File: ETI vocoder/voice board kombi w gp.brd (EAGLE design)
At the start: 160 x 60.3 mm, 174 parts, among them IC1 TL072P, IC1. TL072P, IC2 TL072P, IC2. TL072P, IC3 TL081P, IC3. TL081P, IC4 TL081P, IC4. TL081P, IC5 TL072P, IC6 LM13600AN, IC7 TL072P, IC7. TL072P, P1 C-OR-R050_075-025X100, P1. C-OR-R050_075-025X100, P10 C-OR-R050_075-025X100, P10. C-OR-R050_075-025X100, P11 C-OR-R050_075-025X100, P11. C-OR-R050_075-025X100, P12 C-OR-R050_075-025X100, P12. C-OR-R050_075-025X100, P13 C-OR-R050_075-025X100, P13. C-OR-R050_075-025X100, P14 C-OR-R050_075-025X100, P14. C-OR-R050_075-025X100, P15 C-OR-R050_075-025X100, P15. C-OR-R050_075-025X100, P16 C-OR-R050_075-025X100, P16. C-OR-R050_075-025X100, P2 C-OR-R050_075-025X100, P2. C-OR-R050_075-025X100, P3 C-OR-R050_075-025X100, P3. C-OR-R050_075-025X100, P4 C-OR-R050_075-025X100, P4. C-OR-R050_075-025X100, P5 C-OR-R050_075-025X100, P5. C-OR-R050_075-025X100, P6 C-OR-R050_075-025X100, P6. C-OR-R050_075-025X100, P7 C-OR-R050_075-025X100, P7. C-OR-R050_075-025X100, P8 C-OR-R050_075-025X100, P8. C-OR-R050_075-025X100, P9 C-OR-R050_075-025X100, P9. C-OR-R050_075-025X100, Q1 BF244C, Q1. BF244C, Q2 BC212L, Q2. BC212L

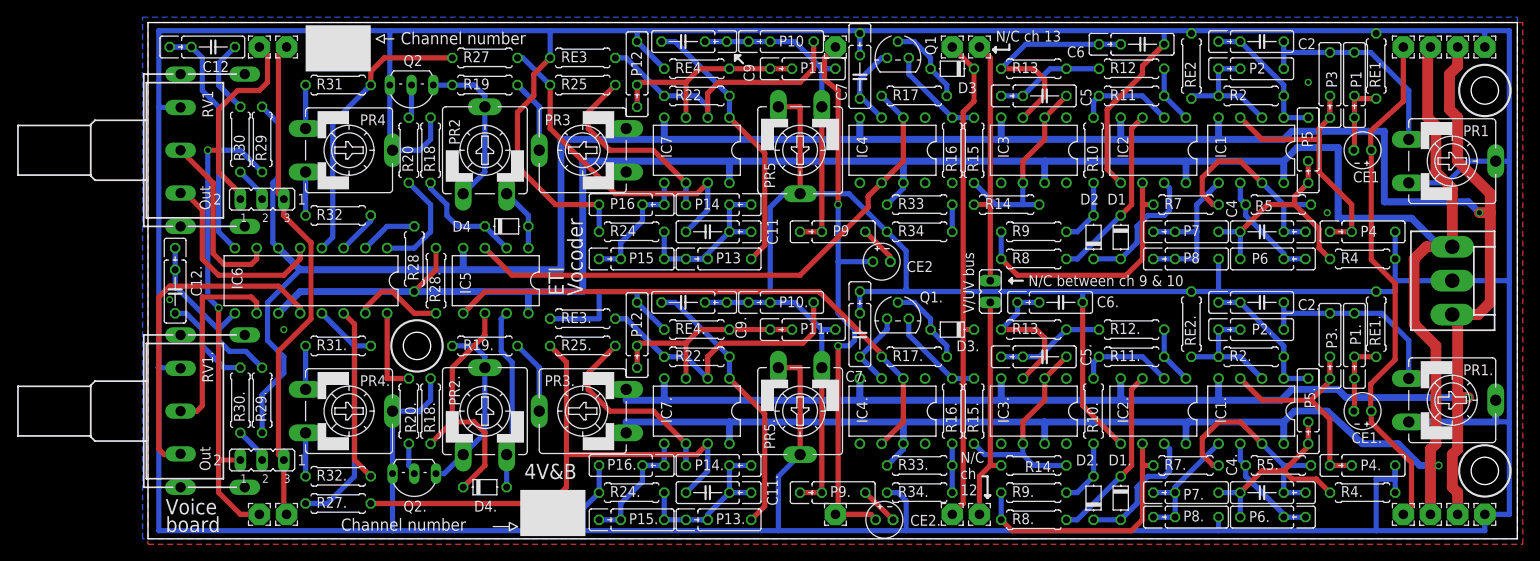
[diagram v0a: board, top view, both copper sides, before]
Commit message: Renamed components to better match parts list from the article. Any part that is not consistent across HP/LP/BP now has either CE, RE or P prefix
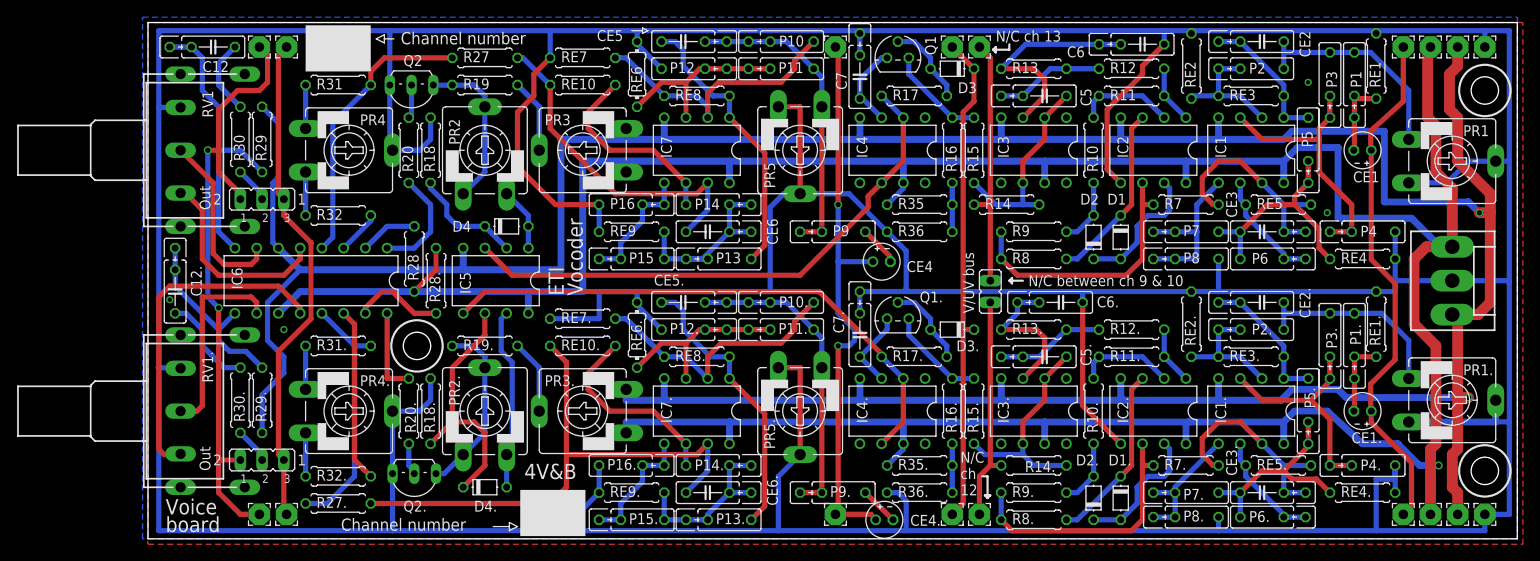
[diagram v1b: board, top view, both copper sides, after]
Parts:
- removed C2, C2.: (no value), joakim:C050_075-025X100J
- removed R2, R2., R4, R4.: (no value), resistor:0207/7
- added CE4, CE4.: (no value), resistor:E2-4
- added RE6, RE6.: (no value), resistor:0204/7
- added RE7, RE7.: (no value), resistor:0207/7
- CE2, CE2.: device resistor:E2-4 -> joakim:C050_075-025X100J
- moved RE4 80.9 mm to (141.9, 32.7), turned to 180 degrees
- moved RE4. 80.1 mm to (141.9, 5.40), turned to 180 degrees
- moved RE3 78.2 mm to (128.9, 51.8)
- moved RE3. 78.2 mm to (128.9, 21.3)
- moved CE2 51.4 mm to (130.2, 58.1), turned to 180 degrees
- moved CE2. 50.9 mm to (130.2, 27.6), turned to 180 degrees
- moved P12 6.70 mm to (63.8, 54.9), turned to 0 degrees
- moved P12. 6.70 mm to (63.8, 24.4), turned to 0 degrees
- moved P11 2.54 mm to (74.0, 54.9)
- moved P11. 2.54 mm to (74.0, 24.4)
- renumbered C11 to CE6, C11. to CE6., C4 to CE3, C4. to CE3., C9 to CE5, C9. to CE5., R22 to RE8, R22. to RE8., R24 to RE9, R24. to RE9., R25 to RE10, R25. to RE10., R33 to R35, R33. to R35., R34 to R36, R34. to R36., R5 to RE5, R5. to RE5.
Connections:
- net EXCITATION_IN: now also CE4.+, CE4..+; no longer CE2.+, CE2..+
- net GND: now also RE6..1, RE6.1, RE7..1, RE7.1; no longer R4..1, R4.1, RE3..1, RE3.1
- net N$1: now also RE3.1; no longer R2.1
- net N$2: now also CE2.1; no longer C2.1
- net N$29: now also RE7.2; no longer RE3.2
- net N$3: now also CE2.2, CE2.3, RE3.2; no longer C2.2, C2.3, R2.2
- net N$45: now also CE4.-; no longer CE2.-
- net N$46: now also RE6.2; no longer RE4.2
- net N$47: now also RE3..1; no longer R2..1
- net N$48: now also CE2..1; no longer C2..1
- net N$49: now also CE2..2, CE2..3, RE3..2; no longer C2..2, C2..3, R2..2
- net N$5: now also RE4.2; no longer R4.2
- net N$50: now also RE4..2; no longer R4..2
- net N$75: now also RE7..2; no longer RE3..2
- net N$90: now also CE4..-; no longer CE2..-
- net N$91: now also RE6..2; no longer RE4..2
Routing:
- net N$91: track 25.6 -> 21.5 mm
- net N$46: track 25.6 -> 21.5 mm
- net BIAS: track 3.18 -> 5.72 mm
- net N$27: track 38.1 -> 36.0 mm
- net N$73: track 38.1 -> 36.0 mm
- net N$75: track 33.3 -> 31.8 mm
- net N$76: track 32.0 -> 33.3 mm
- net N$29: track 34.0 -> 32.7 mm
- net N$30: track 32.0 -> 33.1 mm
- net EXCITATION_IN: track 67.6 -> 66.6 mm

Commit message: Separated LP/BP from BP/HP channels (left channel is never HP, right is never LP). Removed unused/shorted parts. Replaced all caps with wider ones w. 5mm pitch (may have to make them even wider). Replaced parts in left/right channel that had P footprints with R or C if they are now only one type combined with either N/C or short.
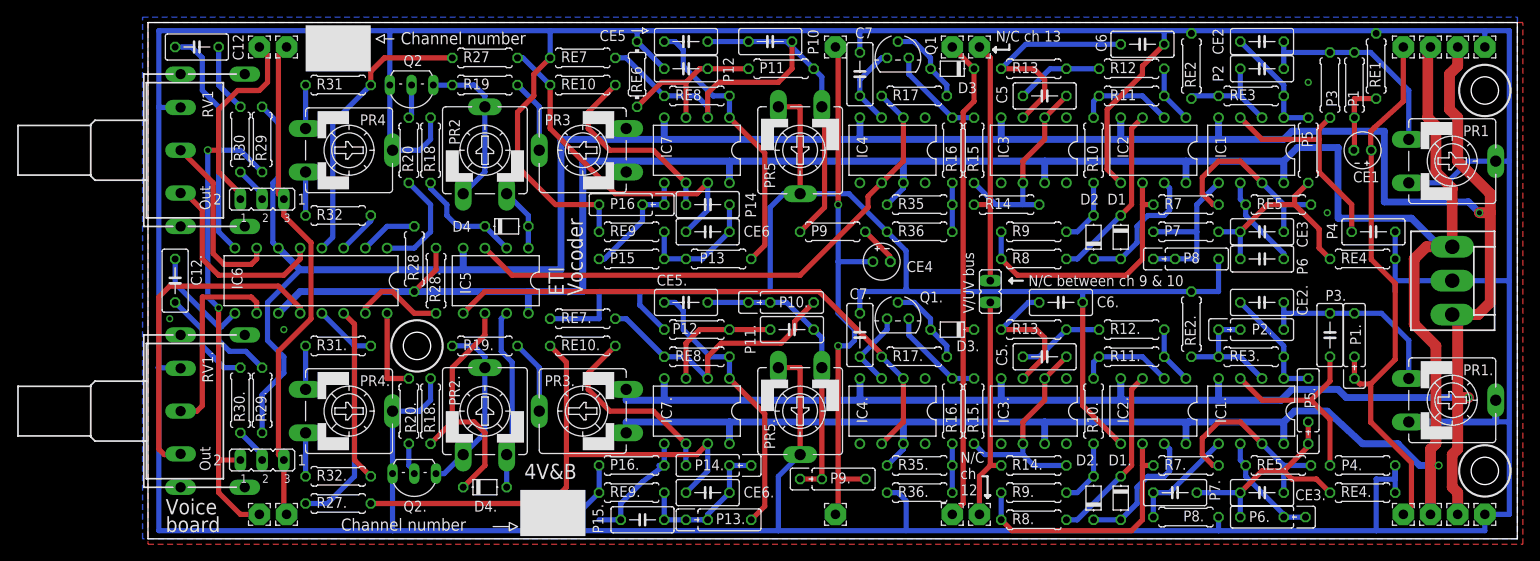
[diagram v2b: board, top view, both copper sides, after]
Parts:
- removed CE1., CE4.: (no value), resistor:E2-4
- removed RE1.: (no value), resistor:0207/7
- removed RE6.: (no value), resistor:0204/7
- C12, C12., C5, C5., C6, C6., C7, C7., CE2, CE2., CE3, CE3., CE5, CE5., CE6, CE6.: device joakim:C050_075-025X100J -> resistor:C050-030X075
- P1, P11, P12., P13, P15, P16., P3, P4., P5, P7, P8., P9: value C-OR-R050_075-025X100 -> (none); device joakim:P050_075-025X100J -> resistor:0207/7
- P10, P11., P12, P14, P15., P2, P3., P4, P6, P7.: value C-OR-R050_075-025X100 -> (none); device joakim:P050_075-025X100J -> resistor:C050-030X075
- moved C12 1.91 mm to (5.71, 57.5)
- moved P9. 1.59 mm to (80.0, 6.99)
- moved P10 1.27 mm to (72.7, 58.1)
- moved P2 1.27 mm to (130.2, 54.9)
- moved C12. 1.27 mm to (3.17, 30.2)
- moved P3. 1.27 mm to (138.1, 23.8)
- moved P11. 1.27 mm to (75.2, 24.4)
- moved P14 1.27 mm to (65.4, 39.1)
- moved P15. 1.27 mm to (57.8, 2.22)
- moved P7. 1.27 mm to (120.0, 5.40)
- moved P4 1.27 mm to (143.2, 35.9)
- moved P6 1.27 mm to (130.2, 32.7)
- moved P12 0.95 mm to (62.9, 54.9)
- moved CE5 0.32 mm to (62.9, 58.1)
- moved CE5. 0.32 mm to (62.9, 27.6)
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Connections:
- removed net N$88: CE1..-, P1..2, P1..3, RE1..2
- removed net N$90: CE4..-, P9..1
- net EXCITATION_IN: now also P9..1; no longer CE4..+
- net GND: no longer C7..3, C7.3, RE1..1, RE6..1
- net N$1: no longer P2.3
- net N$14: no longer C5.3
- net N$16: no longer C6.3
- net N$27: no longer CE5.3, P10.3, P9.3
- net N$28: no longer CE6.3, P13.3, P14.3
- net N$3: no longer CE2.3
- net N$32: no longer P15.3
- net N$33: no longer C12.3
- net N$43: no longer P1.3
- net N$44: no longer P3.3, P4.3
- net N$46: no longer P11.3, P12.3
- net N$49: no longer CE2..3
- net N$5: no longer P5.3
- net N$52: no longer P7..3, P8..3
- net N$53: no longer CE3..3
- net N$6: no longer P6.3
- net N$60: no longer C5..3
- net N$62: no longer C6..3
- net N$7: no longer P7.3
- net N$73: no longer CE5..3
- net N$74: no longer CE6..3
- net N$8: no longer CE3.3
- net N$84: no longer C12..3
- net N$87: no longer P15..3, P16..3
- net N$89: no longer P3..3, P4..3
- net N$91: no longer P11..3, P12..3, RE6..2
- net SPEECH_IN: now also P1..2, P1..3; no longer CE1..+
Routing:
- net GND: track 814.6 -> 793.8 mm
- net N$88: track 8.95 -> 0.00 mm
- net N$28: track 23.5 -> 15.3 mm
- net N$91: track 21.5 -> 14.6 mm
- net N$44: track 30.8 -> 25.7 mm
- net SPEECH_IN: track 61.3 -> 66.0 mm
- net N$90: track 4.54 -> 0.00 mm
- net N$52: track 15.8 -> 12.8 mm
- net N$74: track 21.4 -> 18.8 mm
- net N$60: track 12.7 -> 10.2 mm
- net N$49: track 16.4 -> 13.9 mm
- net N$3: track 16.4 -> 13.9 mm
- net N$14: track 12.7 -> 10.2 mm
- net N$1: track 15.3 -> 12.8 mm
- net N$5: track 27.2 -> 24.6 mm
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
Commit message: Changed all caps and C-or-Rs for 5mm pitch 3mm wide ones
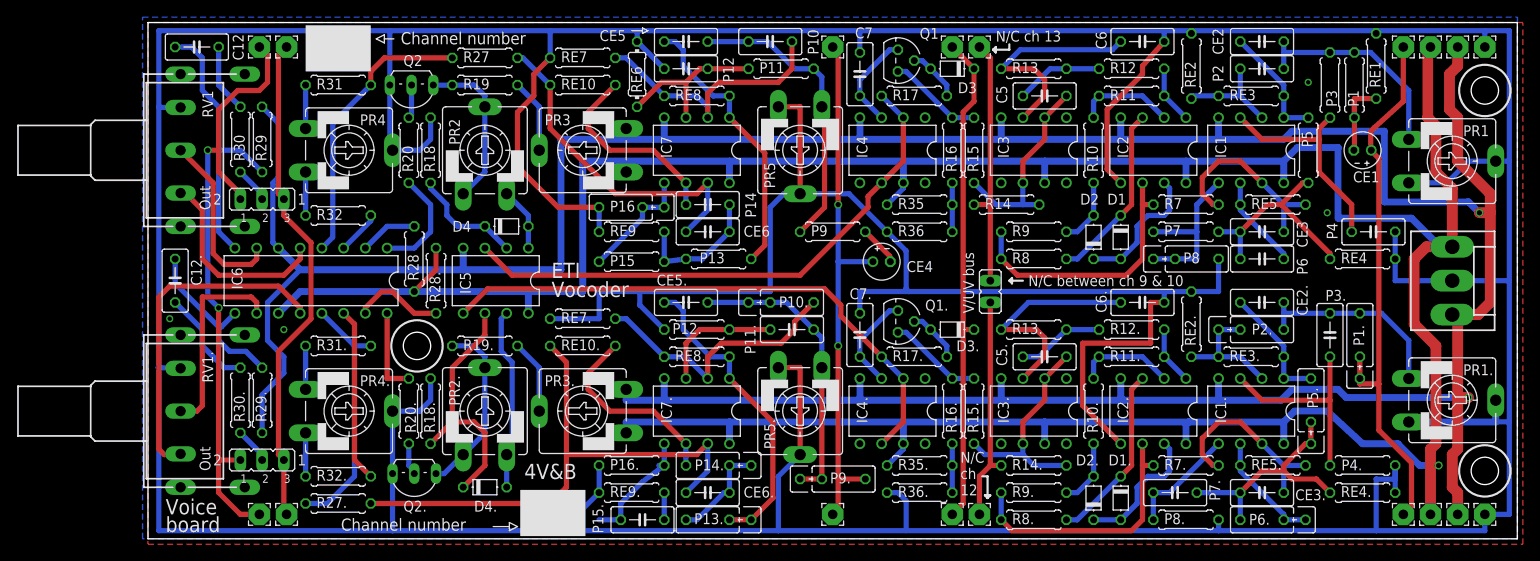
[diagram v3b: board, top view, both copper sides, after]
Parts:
- P1., P10., P13., P14., P16, P2., P5., P6., P8, P9.: value C-OR-R050_075-025X100 -> C-OR-R050_075-030X100; device joakim:P050_075-025X100J -> joakim:P050_075-030X100J
- moved C6. 9.52 mm to (116.2, 27.6)
- moved RE5 0.64 mm to (131.4, 39.1)
- moved RE5. 0.64 mm to (131.4, 8.57)
- moved P1. 0.63 mm to (141.6, 22.5)
- moved C6 0.32 mm to (116.2, 58.1)
- moved P15 0.32 mm to (56.5, 32.4)
- moved P16 0.32 mm to (56.5, 38.7)
- moved Q1. 0.32 mm to (87.6, 25.4), turned to 270 degrees
- moved P6. 0.32 mm to (131.4, 2.22)
- moved P8. 0.32 mm to (121.3, 2.22)
- moved P5. 0.32 mm to (135.9, 14.9)
- moved PAD3 0.32 mm to (80.0, 57.5)
- moved PAD4 0.32 mm to (80.0, 2.86)
- moved Q1 0.32 mm to (87.6, 55.9), turned to 270 degrees
- turned P13. to 0 degrees
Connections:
- new net N$88: P15..1, RE9..2
- net N$74: now also P13..1; no longer P13..2, P13..3, P15..1, RE9..2
- net N$76: now also P13..2, P13..3; no longer P13..1
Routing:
- net N$62: track 17.0 -> 26.6 mm
- net GND: track 793.8 -> 801.4 mm
- net N$74: track 18.8 -> 12.1 mm
- net N$65: track 9.83 -> 6.26 mm
- net N$19: track 9.83 -> 6.26 mm
- net N$76: track 33.0 -> 36.3 mm
- net N$88: track 0.00 -> 3.17 mm
- net N$64: track 9.35 -> 11.4 mm
- net SPEECH_IN: track 66.0 -> 64.3 mm
- net EXCITATION_IN: track 64.8 -> 63.1 mm
- net N$18: track 9.72 -> 11.4 mm
- net N$66: track 65.6 -> 66.4 mm
- net N$50: track 27.4 -> 28.2 mm
- net N$8: track 23.1 -> 22.5 mm
- net N$53: track 23.1 -> 22.5 mm
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
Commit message: Finished capacitor spacing tweaks, ic sockets should fit now
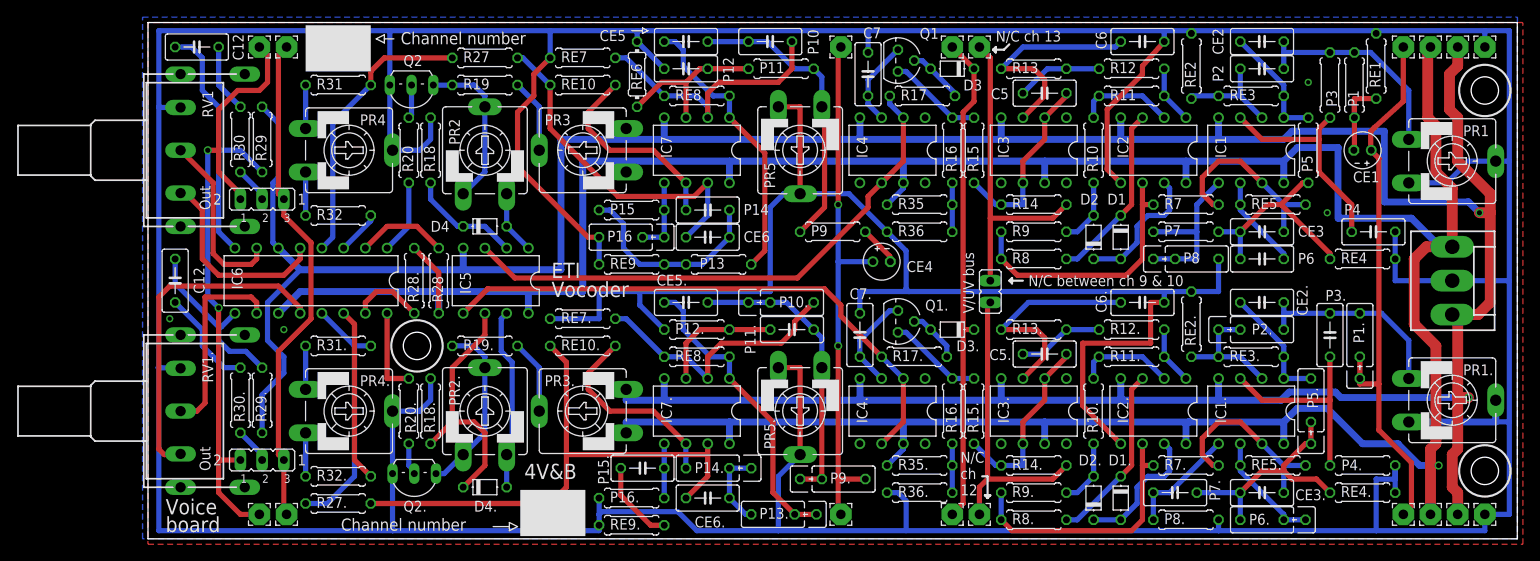
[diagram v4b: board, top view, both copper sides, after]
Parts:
- moved P13. 7.65 mm to (74.3, 2.86)
- moved P15. 6.03 mm to (57.8, 8.26), turned to 0 degrees
- moved P15 6.03 mm to (56.5, 38.4), turned to 0 degrees
- moved R28 3.82 mm to (34.0, 30.2)
- moved RE9. 3.81 mm to (56.5, 1.59)
- moved P16. 3.81 mm to (56.5, 4.76)
- moved RE9 3.81 mm to (56.5, 32.1)
- moved P16 3.49 mm to (56.5, 35.2)
- moved R14 3.17 mm to (103.5, 39.1), turned to 0 degrees
- moved R28. 2.54 mm to (31.1, 30.2)
- moved D4 2.54 mm to (39.4, 36.5)
- moved C7 0.95 mm to (84.1, 54.3)
- moved PAD3 0.95 mm to (81.0, 57.5)
- moved PAD4 0.95 mm to (81.0, 2.86)
- moved R17 0.95 mm to (90.5, 51.8)
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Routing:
- net VU_DETECTOR_2: track 26.6 -> 35.2 mm
- net N$28: track 15.6 -> 24.0 mm
- net N$87: track 14.4 -> 6.35 mm
- net VU_DETECTOR: track 29.7 -> 37.4 mm
- net N$88: track 3.17 -> 9.70 mm
- net +12V: track 368.9 -> 374.4 mm
- net N$32: track 13.9 -> 8.89 mm
- net N$40: track 12.6 -> 8.67 mm
- net N$38: track 6.77 -> 10.7 mm
- net N$61: track 25.4 -> 21.9 mm
- net N$74: track 12.1 -> 9.36 mm
- net N$80: track 10.7 -> 8.56 mm
- net N$15: track 23.5 -> 21.9 mm
- net N$18: track 11.4 -> 10.0 mm
- net GND: track 801.4 -> 800.4 mm
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
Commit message: Centered capacitors on resistors for a (hopefully) more tidy look
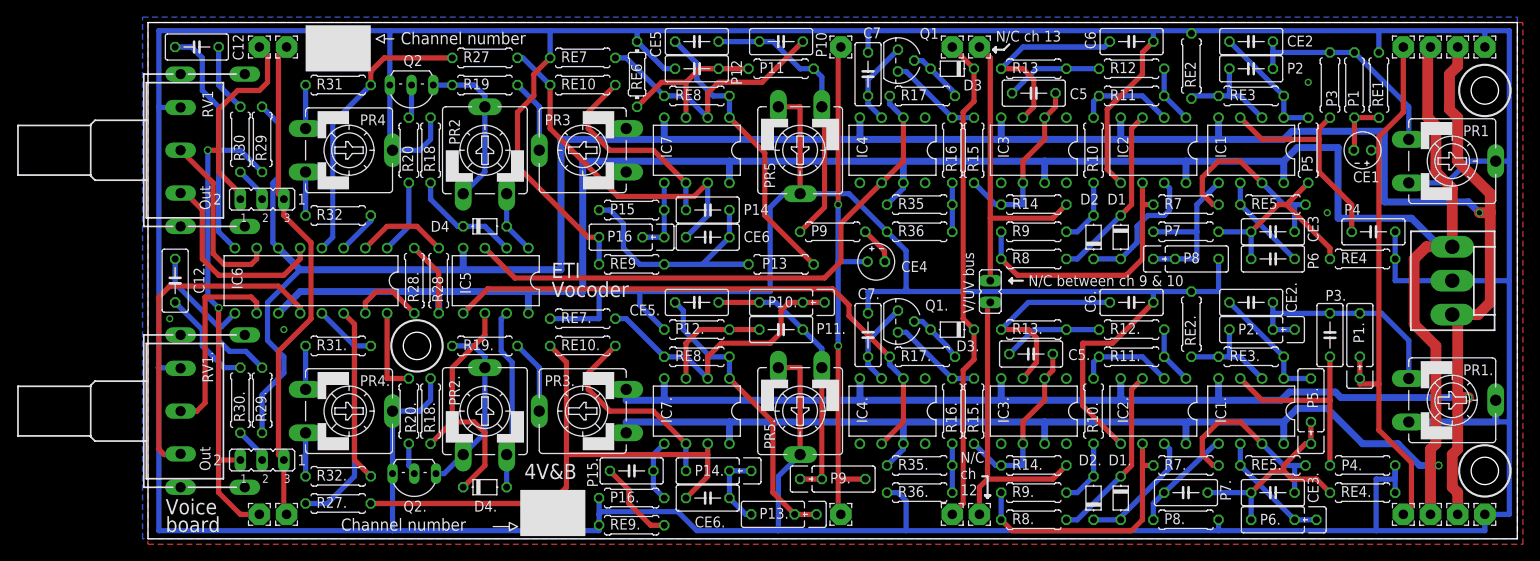
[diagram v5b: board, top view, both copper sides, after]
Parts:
- moved P13 7.30 mm to (74.0, 32.1)
- moved RE1 2.25 mm to (143.8, 53.0)
- moved C5. 1.59 mm to (103.2, 21.6)
- moved P15. 1.31 mm to (56.5, 7.94)
- moved C5 1.27 mm to (103.5, 52.1)
- moved CE2 1.27 mm to (128.9, 58.1)
- moved CE2. 1.27 mm to (128.9, 27.6)
- moved P10 1.27 mm to (74.0, 58.1)
- moved P2 1.27 mm to (128.9, 54.9)
- moved P2. 1.27 mm to (130.2, 24.4), turned to 0 degrees
- moved P6. 1.27 mm to (132.7, 2.22)
- moved CE5 1.27 mm to (64.1, 58.1)
- moved CE5. 1.27 mm to (64.1, 27.6)
- moved P12 1.27 mm to (64.1, 54.9)
- moved C6 1.27 mm to (114.9, 58.1)
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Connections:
- net N$47: now also P2..1; no longer P2..2, P2..3
- net N$48: now also P2..2, P2..3; no longer P2..1
- net N$73: now also P10..1; no longer P10..2, P10..3
- net N$75: now also P10..2, P10..3; no longer P10..1
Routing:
- net N$28: track 24.0 -> 34.8 mm
- net N$43: track 11.2 -> 6.73 mm
- net N$48: track 23.5 -> 27.4 mm
- net N$16: track 26.4 -> 23.3 mm
- net N$62: track 26.6 -> 23.9 mm
- net N$47: track 15.0 -> 12.5 mm
- net N$75: track 31.8 -> 34.0 mm
- net N$73: track 34.1 -> 32.1 mm
- net GND: track 800.4 -> 798.5 mm
- net N$20: track 65.0 -> 66.9 mm
- net N$60: track 10.1 -> 11.7 mm
- net N$64: track 11.4 -> 10.0 mm
- net N$29: track 31.5 -> 30.2 mm
- net N$91: track 14.6 -> 13.4 mm
- net N$27: track 34.5 -> 33.2 mm
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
